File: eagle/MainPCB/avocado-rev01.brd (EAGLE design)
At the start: 100 x 60 mm, 10 parts, among them J1 10118194-0001LF, J2 CON-DSUB-15-VGA, J3 0475710001, U1 V3S

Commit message: updated schematic
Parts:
- added D1: LL-R3528RGBC-008-B, LL-R3528RGBC-008-B:LED_LL-R3528RGBC-008-B
- added R1, R2, R3: (no value), resistor:R0603
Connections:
- new net N$10: D1.2, R3.2
- new net N$11: D1.3, R2.1
- new net N$7: R1.2, U1.77
- new net N$8: R2.2, U1.78
- new net N$9: D1.4, R1.1
- net GND: now also R3.1
- net VCC: now also D1.1
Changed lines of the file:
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@@
 <attribute name="VALUE" x="26.39323125" y="-0.3052" size="1.271540625" layer="27"/>
+</element>
+<element name="D1" library="LL-R3528RGBC-008-B" package="LED_LL-R3528RGBC-008-B" value="LL-R3528RGBC-008-B" x="0" y="-11" smashed="yes">
+<attribute name="AVAILABILITY" value="Unavailable" x="0" y="-11" size="1.778" layer="27" display="off"/>
+<attribute name="DESCRIPTION" value=" LED; SMD; 3528, PLCC2; RGB; 3.5x2.8mm; 120°; Red lumin: 1 " x="0" y="-11" size="1.778" layer="27" display="off"/>
+<attribute name="MF" value="Lucky Light" x="0" y="-11" size="1.778" layer="27" display="off"/>
+<attribute name="MP" value="LL-R3528RGBC-008-B" x="0" y="-11" size="1.778" layer="27" display="off"/>
+<attribute name="NAME" x="-2.55938125" y="-8.44061875" size="1.778959375" layer="25"/>
+<attribute name="PACKAGE" value="PLCC-2 Lucky Light" x="0" y="-11" size="1.778" layer="27" display="off"/>
+<attribute name="PRICE" value="None" x="0" y="-11" size="1.778" layer="27" display="off"/>
+<attribute name="VALUE" x="-2.562490625" y="-14.788859375" size="1.779790625" layer="27"/>
+</element>
+<element name="R1" library="resistor" library_urn="urn:adsk.eagle:library:348" package="R0603" package3d_urn="urn:adsk.eagle:package:26057/1" value="" x="-1" y="-18" smashed="yes">
+<attribute name="NAME" x="-1.635" y="-17.365" size="1.27" layer="25"/>
+<attribute name="VALUE" x="-1.635" y="-19.905" size="1.27" layer="27"/>
+</element>
+<element name="R2" library="resistor" library_urn="urn:adsk.eagle:library:348" package="R0603" package3d_urn="urn:adsk.eagle:package:26057/1" value="" x="-1" y="-22" smashed="yes">
+<attribute name="NAME" x="-1.635" y="-21.365" size="1.27" layer="25"/>
+<attribute name="VALUE" x="-1.635" y="-23.905" size="1.27" layer="27"/>
+</element>
+<element name="R3" library="resistor" library_urn="urn:adsk.eagle:library:348" package="R0603" package3d_urn="urn:adsk.eagle:package:26057/1" value="" x="-1" y="-26" smashed="yes">
+<attribute name="NAME" x="-1.635" y="-25.365" size="1.27" layer="25"/>
+<attribute name="VALUE" x="-1.635" y="-27.905" size="1.27" layer="27"/>
 </element>
 </elements>
@@
 <contactref element="J3" pad="10"/>
 <contactref element="J3" pad="13"/>
+<contactref element="R3" pad="1"/>
 <wire x1="18.85" y1="28" x2="18.85" y2="30" width="0" layer="19" extent="1-1"/>
 <wire x1="18.85" y1="26" x2="18.85" y2="28" width="0" layer="19" extent="1-1"/>
@@
 <wire x1="26.775" y1="1.775" x2="26.775" y2="4.365" width="0" layer="19" extent="1-1"/>
 <wire x1="37.175" y1="3.925" x2="26.775" y2="4.365" width="0" layer="19" extent="1-1"/>
+<wire x1="-1.85" y1="-26" x2="26.775" y2="1.775" width="0" layer="19" extent="1-1"/>
 </signal>
 <signal name="N$1">
@@
 <signal name="VCC">
 <contactref element="J1" pad="1"/>
+<contactref element="D1" pad="1"/>
+<wire x1="-1.4" y1="-11.85" x2="4.7" y2="31.3" width="0" layer="19" extent="1-1"/>
 </signal>
 <signal name="USB-ID">
@@
 <contactref element="J3" pad="6"/>
 </signal>
+<signal name="N$7">
+<contactref element="U1" pad="77"/>
+<contactref element="R1" pad="2"/>
+<wire x1="-0.15" y1="-18" x2="45.6159375" y2="36.363959375" width="0" layer="19" extent="1-1"/>
+</signal>
+<signal name="N$8">
+<contactref element="U1" pad="78"/>
+<contactref element="R2" pad="2"/>
+<wire x1="-0.15" y1="-22" x2="45.33309375" y2="36.081115625" width="0" layer="19" extent="1-1"/>
+</signal>
+<signal name="N$10">
+<contactref element="D1" pad="2"/>
+<contactref element="R3" pad="2"/>
+<wire x1="1.4" y1="-11.85" x2="-0.15" y2="-26" width="0" layer="19" extent="1-1"/>
+</signal>
+<signal name="N$11">
+<contactref element="D1" pad="3"/>
+<contactref element="R2" pad="1"/>
+<wire x1="1.4" y1="-10.15" x2="-1.85" y2="-22" width="0" layer="19" extent="1-1"/>
+</signal>
+<signal name="N$9">
+<contactref element="R1" pad="1"/>
+<contactref element="D1" pad="4"/>
+<wire x1="-1.4" y1="-10.15" x2="-1.85" y2="-18" width="0" layer="19" extent="1-1"/>
+</signal>
 </signals>

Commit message: Connected power
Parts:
- added C10, C15, C5: 1u, marius:C0603
- added C11, C14, C16, C19, C6, C9: 100n, marius:C0603
- added C12, C13, C17, C18, C7, C8: 22u, marius:CAP4.3X6.1
- added FID1, FID2: FIDUCIAL, marius:FIDUCIAL_1MM
- added L1, L2, L3: CALC, marius:B82462A4153K
- added P2: CONNECTOR-15686115148922, marius:686115148922
- added P3: PADTH, marius:PAD
- added R10, R11, R14, R15, R6, R7: CALC, marius:R0603
- added R12, R4, R8: 100k, marius:R0603
- added R13, R5, R9: 59k, marius:R0603
- added R16: 0, marius:R0603
- added TP1: TEST_TESTPOINT, marius:TEST_TESTPOINT
- added U2, U3, U4: AP65111A, marius:TSOT26
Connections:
- new net 1V2: C18.1, C19.1, L3.P$2, R14.1, U1.108, U1.126, U1.19, U1.20, U1.21, U1.25, U1.26, U1.38, U1.47, U1.51, U1.56, U1.58, U1.64, U1.80, U1.88
- new net 1V8: C13.1, C14.1, L2.P$2, R10.1, U1.59, U1.60, U1.61, U1.62, U1.65, U1.66, U1.67, U1.68, U1.69, U1.70, U1.72, U1.79
- new net 3V: U1.115, U1.76
- new net 3V3: C8.1, C9.1, L1.P$2, R16.2, R6.1, U1.104, U1.109, U1.12, U1.127, U1.29, U1.50, U1.57, U1.85, U1.93
- new net N$13: R16.1, U1.98
- new net N$15: R5.2, U2.6
- new net N$16: C5.2, L1.P$1, U2.3
- new net N$17: R5.1, R6.2, R7.1
- new net N$18: C5.1, U2.4
- new net N$19: R4.1, U2.5
- new net N$20: R9.2, U3.6
- new net N$21: C10.2, L2.P$1, U3.3
- new net N$22: R10.2, R11.1, R9.1
- new net N$23: C10.1, U3.4
- new net N$25: R8.1, U3.5
- new net N$27: R13.2, U4.6
- new net N$28: C15.2, L3.P$1, U4.3
- new net N$29: R13.1, R14.2, R15.1
- new net N$30: C15.1, U4.4
- new net N$31: R12.1, U4.5
- new net N$34: U1.97
- new net N$42: U1.73
- new net N$43: U1.71
- new net N$44: U1.63
- new net VIN: C11.1, C12.1, C16.1, C17.1, C6.1, C7.1, R12.2, R4.2, R8.2, U2.1, U3.1, U4.1
- net GND: now also C11.2, C12.2, C13.2, C14.2, C16.2, C17.2, C18.2, C19.2, C6.2, C7.2, C8.2, C9.2, R11.2, R15.2, R7.2, U1.116, U1.P$1, U2.2, U3.2, U4.2
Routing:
- net VIN: track 0.00 -> 35.9 mm, vias 0 -> 6
- net 3V3: track 0.00 -> 16.1 mm, vias 0 -> 2
- net 1V8: track 0.00 -> 16.1 mm, vias 0 -> 2
- net 1V2: track 0.00 -> 16.1 mm, vias 0 -> 2
- net GND: track 0.00 -> 13.9 mm, vias 0 -> 9
- net N$28: track 0.00 -> 9.15 mm
- net N$16: track 0.00 -> 9.15 mm
- net N$21: track 0.00 -> 9.15 mm
- net N$3: track 0.00 -> 5.90 mm
- net N$29: track 0.00 -> 3.50 mm
- net N$22: track 0.00 -> 3.50 mm
- net N$17: track 0.00 -> 3.50 mm
- net N$19: track 0.00 -> 3.07 mm
- net N$31: track 0.00 -> 3.07 mm
- net N$25: track 0.00 -> 3.07 mm
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- added copper zone on layer 1, net 1V2
- added copper zone on layer 1, net 1V8
- added copper zone on layer 1, net 3V3
- added copper zone on layer 16, net GND
- added copper zone on layer 1, net VIN

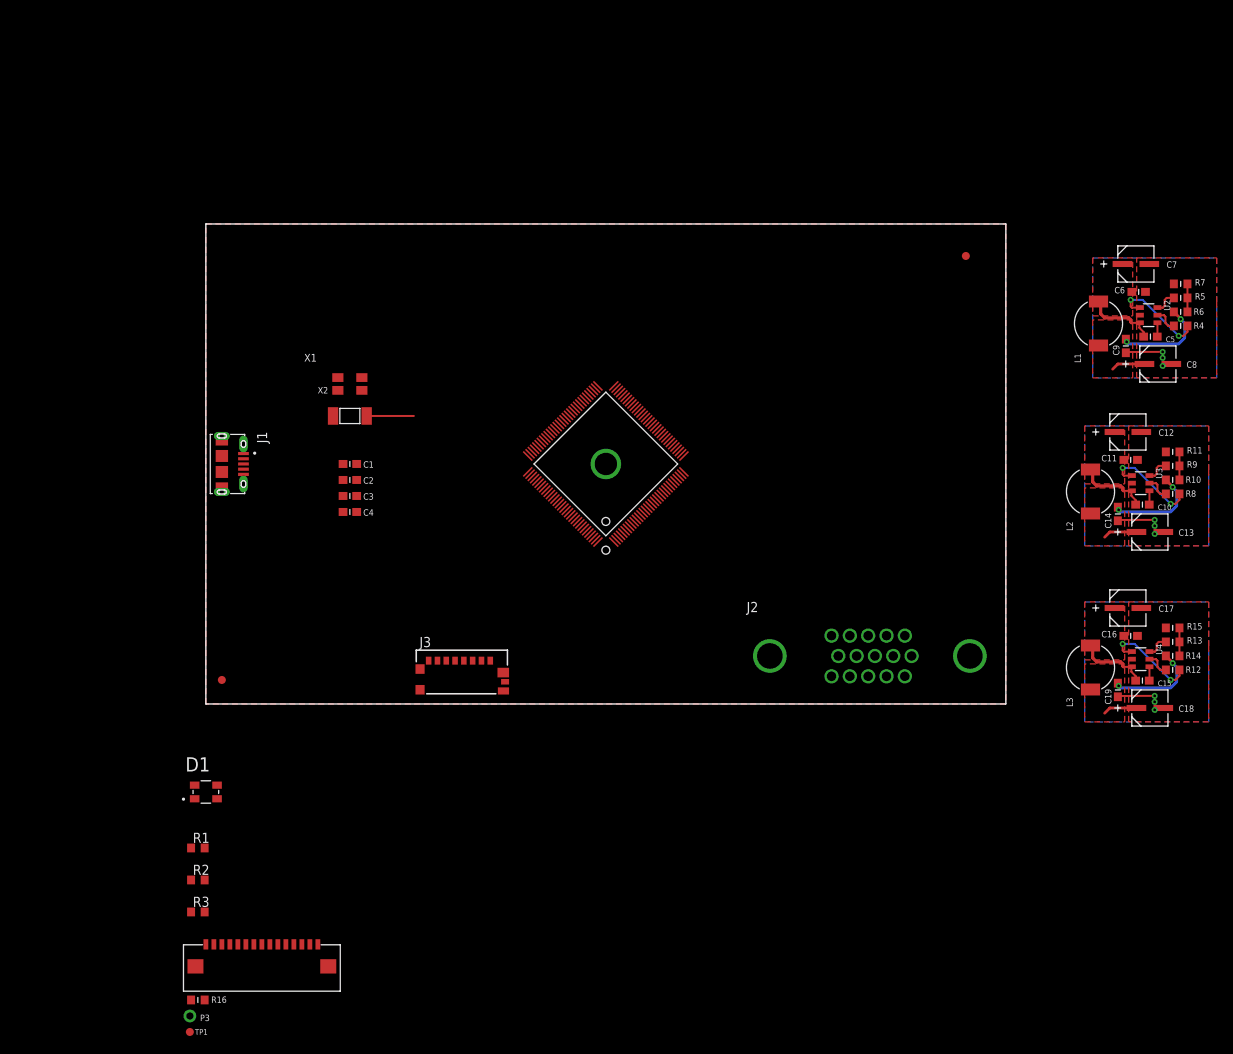
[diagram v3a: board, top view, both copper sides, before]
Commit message: connected sd card and added led
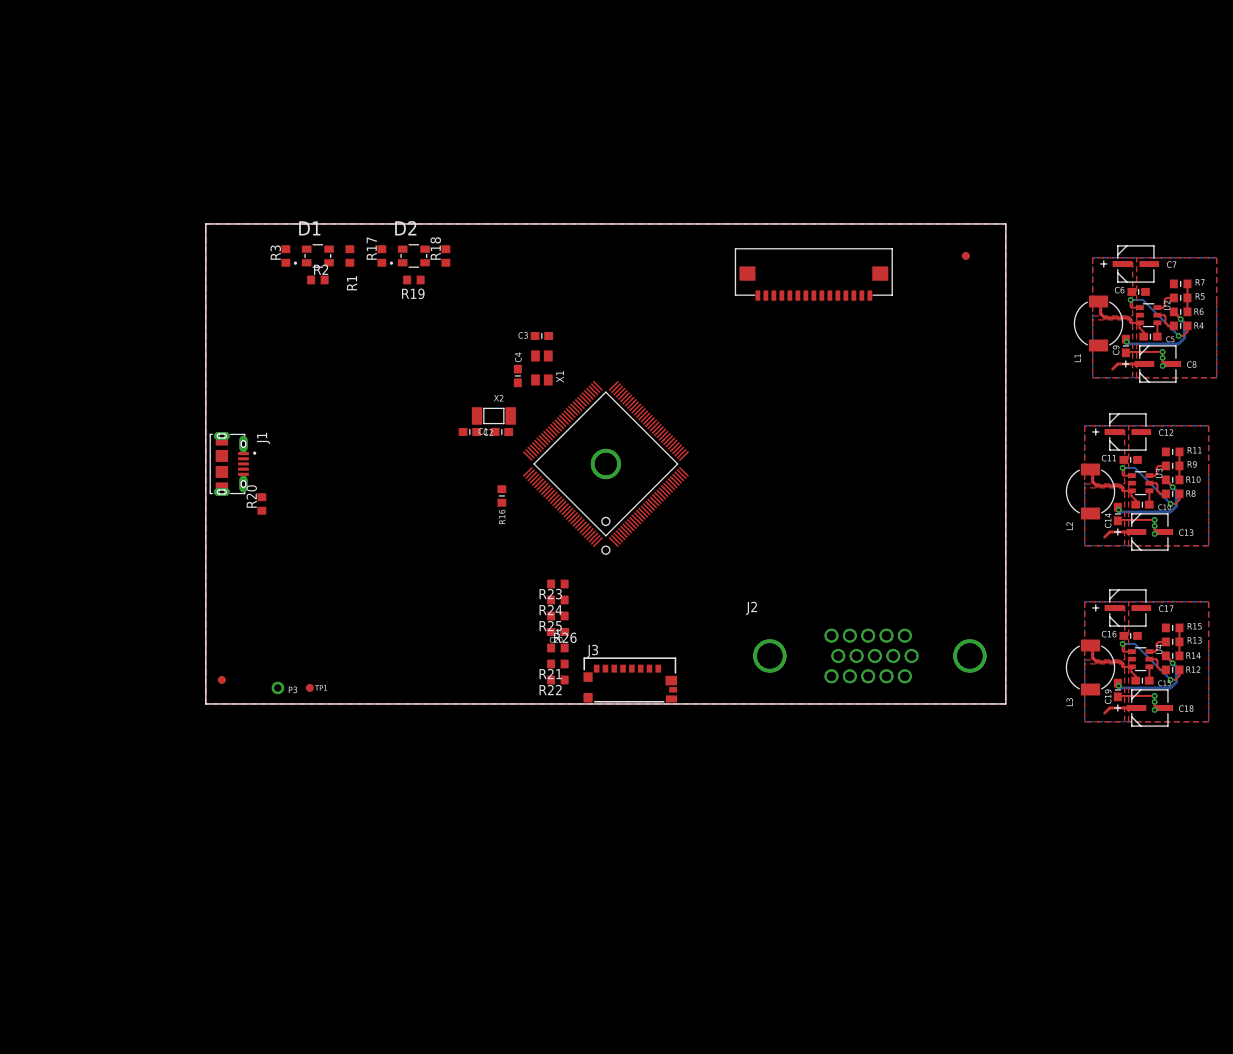
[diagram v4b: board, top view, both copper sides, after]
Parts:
- added C20: 10u, marius:C0603
- added D2: LL-R3528RGBC-008-B, LL-R3528RGBC-008-B:LED_LL-R3528RGBC-008-B
- added R17, R18, R19, R20: (no value), resistor:R0603
- added R21, R22, R23, R24, R25, R26: 47k, resistor:R0603
- moved P2 111.0 mm to (76.0, 54.0), turned to 180 degrees
- moved R3 82.7 mm to (10.0, 56.0), turned to 90 degrees
- moved R2 76.5 mm to (14.0, 53.0)
- moved R1 76.4 mm to (18.0, 56.0), turned to 270 degrees
- moved R16 73.6 mm to (37.0, 26.0), turned to 270 degrees
- moved D1 68.4 mm to (14.0, 56.0)
- moved TP1 45.5 mm to (13.0, 2.00)
- moved P3 42.4 mm to (9.00, 2.00)
- moved C3 31.2 mm to (42.0, 46.0), turned to 180 degrees
- moved C4 27.0 mm to (39.0, 41.0), turned to 90 degrees
- moved X1 24.1 mm to (42.0, 42.0), turned to 270 degrees
- moved J3 21.0 mm to (53.0, 3.00)
- moved C1 19.4 mm to (37.0, 34.0), turned to 180 degrees
- moved X2 18.0 mm to (36.0, 36.0)
- moved C2 16.2 mm to (33.0, 34.0)
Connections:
- net VSS renamed N$46
- removed net VDD: J3.4
- new net N$12: D1.2, R1.2
- new net N$14: D1.3, R2.2
- new net N$24: D1.4, R3.2
- new net N$26: R2.1
- new net N$32: R1.1
- new net N$33: R17.1
- new net N$35: R18.1
- new net N$36: R19.1
- new net N$37: U1.5
- new net N$38: U1.4
- new net N$39: U1.3
- new net N$40: R20.1
- new net N$41: R21.2, R22.2, R23.2, R24.2, R25.2, R26.2
- new net N$45: C20.1, J3.4
- new net SDC0_CLK: J3.5, R26.1, U1.105
- new net SDC0_CMD: J3.3, R25.1, U1.103
- new net SDC0_D0: J3.7, R21.1, U1.106
- new net SDC0_D1: J3.8, R22.1, U1.107
- new net SDC0_D2: J3.1, R23.1, U1.101
- new net SDC0_D3: J3.2, R24.1, U1.102
- net GND: now also C20.2
- net N$10: now also D2.3, R18.2; no longer D1.2, R3.2
- net N$11: now also D2.4, R17.2; no longer D1.3, R2.1
- net N$7: no longer R1.2
- net N$8: no longer R2.2
- net N$9: now also D2.2, R19.2; no longer D1.4, R1.1
- net USB-ID: now also R20.2
- net VCC: now also D2.1
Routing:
- net N$3: track 5.90 -> 0.00 mm

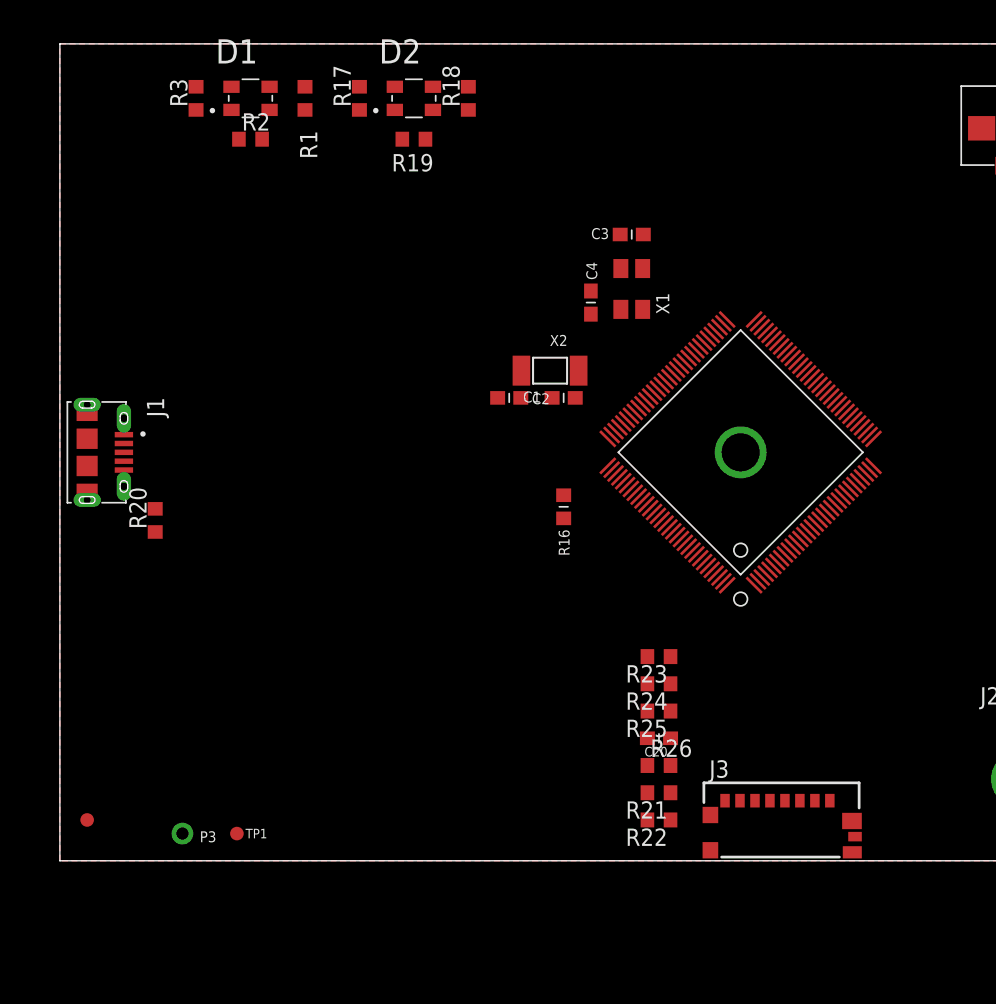
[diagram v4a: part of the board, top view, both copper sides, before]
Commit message: added testpoints
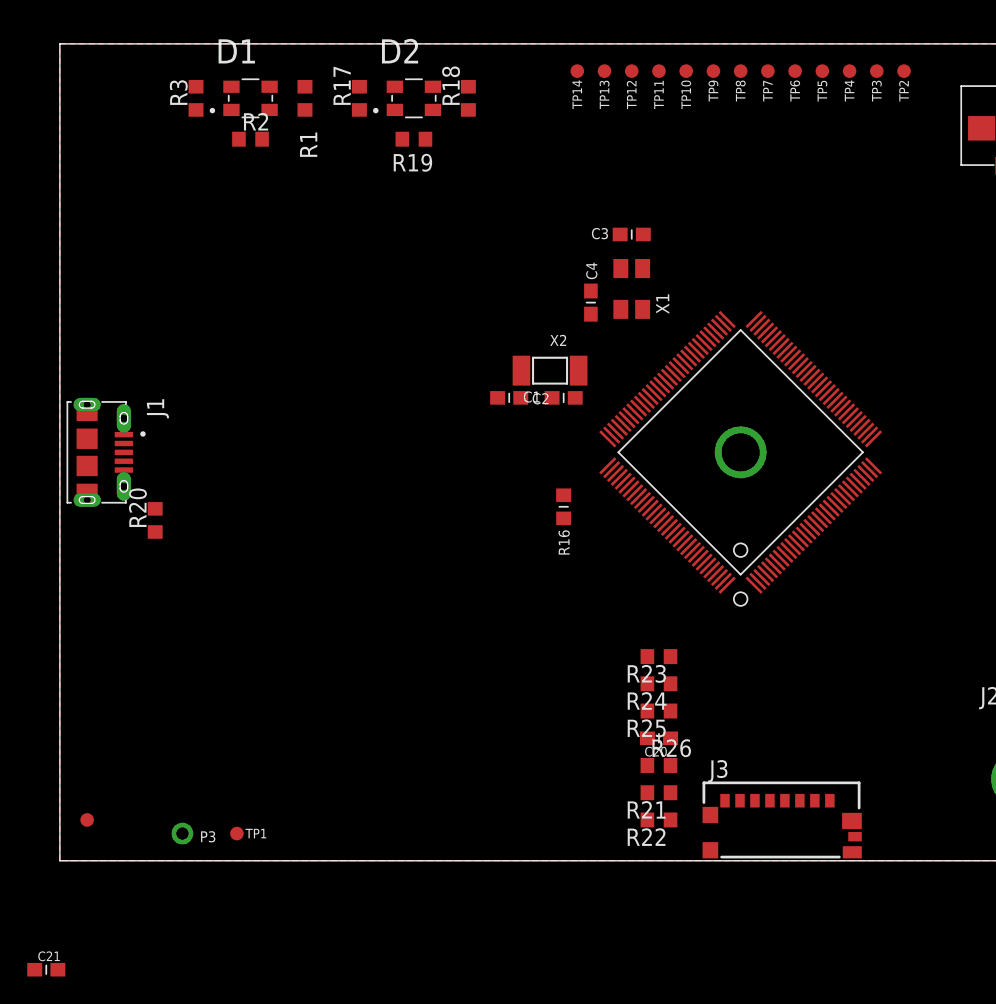
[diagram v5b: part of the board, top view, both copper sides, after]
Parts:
- added C21: 10u, marius:C0603
- added TP10, TP11, TP12, TP13, TP14, TP2, TP3, TP4, TP5, TP6, TP7, TP8, TP9: TEST_TESTPOINT, marius:TEST_TESTPOINT
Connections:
- new net N$47: TP1.1, U1.39
- new net N$48: TP2.1, U1.40
- new net N$49: TP5.1, U1.45
- new net N$50: TP6.1, U1.46
- new net N$51: TP7.1, U1.48
- new net N$52: TP8.1, U1.49
- new net N$53: TP9.1, U1.52
- new net N$54: TP10.1, U1.53
- new net N$55: TP11.1, U1.54
- new net N$56: TP12.1, U1.55
- new net N$57: TP3.1, U1.43
- new net N$58: TP4.1, U1.44
- new net N$59: TP14.1, U1.9
- new net N$60: TP13.1, U1.8
- net GND: now also C21.2
- net VCC: now also C21.1

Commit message: updated i2c
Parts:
- removed P3: PADTH, marius:PAD
- added 5V, GND: PADTH, marius:PAD
- added R27: (no value), resistor:R0603
- added R28, R29, R30, R31: 2k, resistor:R0603
- moved TP1 75.7 mm to (64.0, 58.0)
- moved P2 71.4 mm to (26.0, 3.00), turned to 0 degrees
- moved C21 32.4 mm to (4.00, 24.0), turned to 180 degrees
- moved C1 6.40 mm to (33.0, 39.0), turned to 90 degrees
- moved C2 6.40 mm to (37.0, 39.0), turned to 90 degrees
- moved C20 4.47 mm to (46.0, 5.00), turned to 270 degrees
- moved C4 3.61 mm to (42.0, 39.0), turned to 0 degrees
- moved R21 2.24 mm to (43.0, 7.00)
- moved R22 2.24 mm to (43.0, 5.00)
- moved R26 2.24 mm to (43.0, 9.00)
- moved C3 1.00 mm to (42.0, 45.0)
- moved R23 1.00 mm to (43.0, 15.0)
- moved R24 1.00 mm to (43.0, 13.0)
- moved R25 1.00 mm to (43.0, 11.0)
- moved X2 1.00 mm to (35.0, 36.0), turned to 180 degrees
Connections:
- new net N$61: D1.1
- new net N$62: D2.1
- new net N$63: R27.1, R28.1, R29.1, R30.1, R31.1
- net GND: now also GND.P$1
- net N$49: now also R27.2, R28.2
- net N$50: now also R29.2
- net N$51: now also R30.2
- net N$52: now also R31.2
- net VCC: now also 5V.P$1; no longer D1.1, D2.1
